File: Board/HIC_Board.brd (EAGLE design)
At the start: 52 x 37.5 mm, 104 parts, among them IC1 CXA2075, IC2 4069UBF, IC3 LM358D, IC4 FMW1A, IC5 FMW1A, IC6 IMN10A, Q1 2SA1037, Q2 2SC2411k

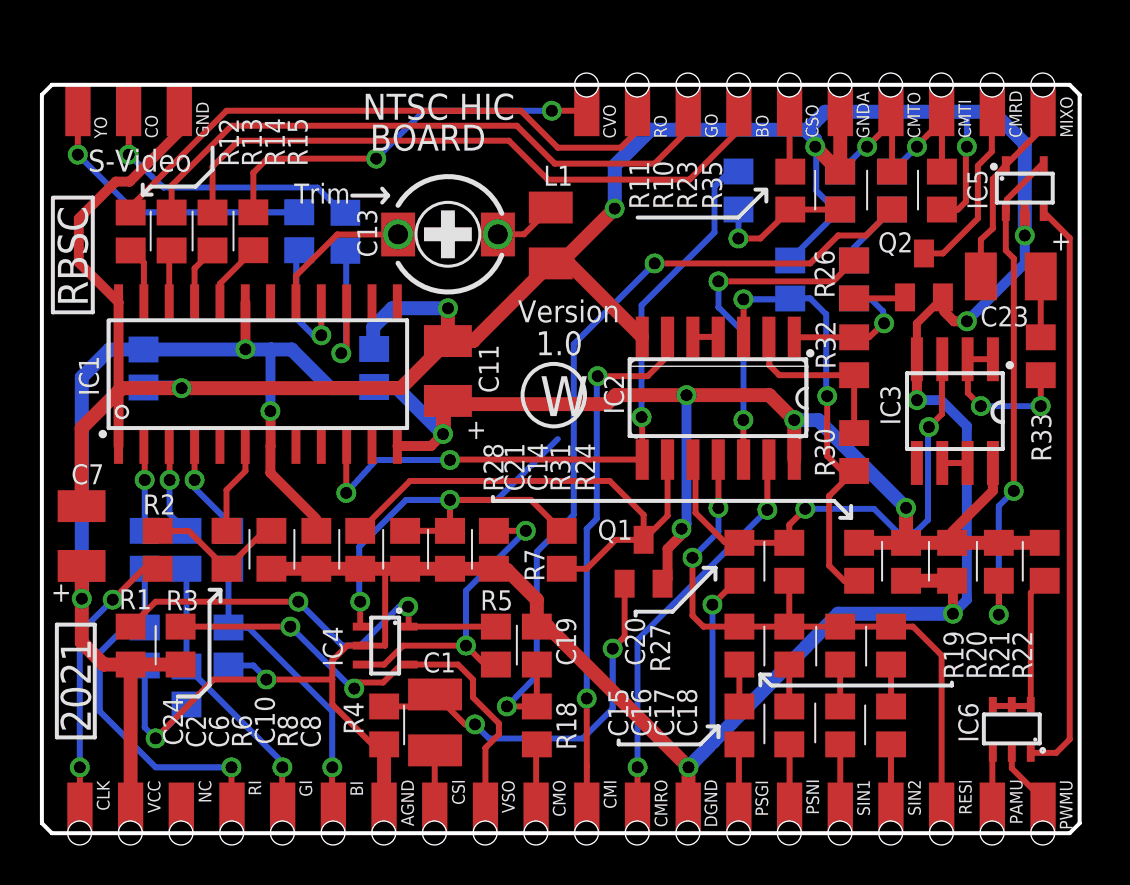
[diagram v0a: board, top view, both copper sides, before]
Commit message: Updated 21.09.2023
Updated to v1.2. The error was fixed, the resistor was added for HB-F1XDJ computer (see the readme file)
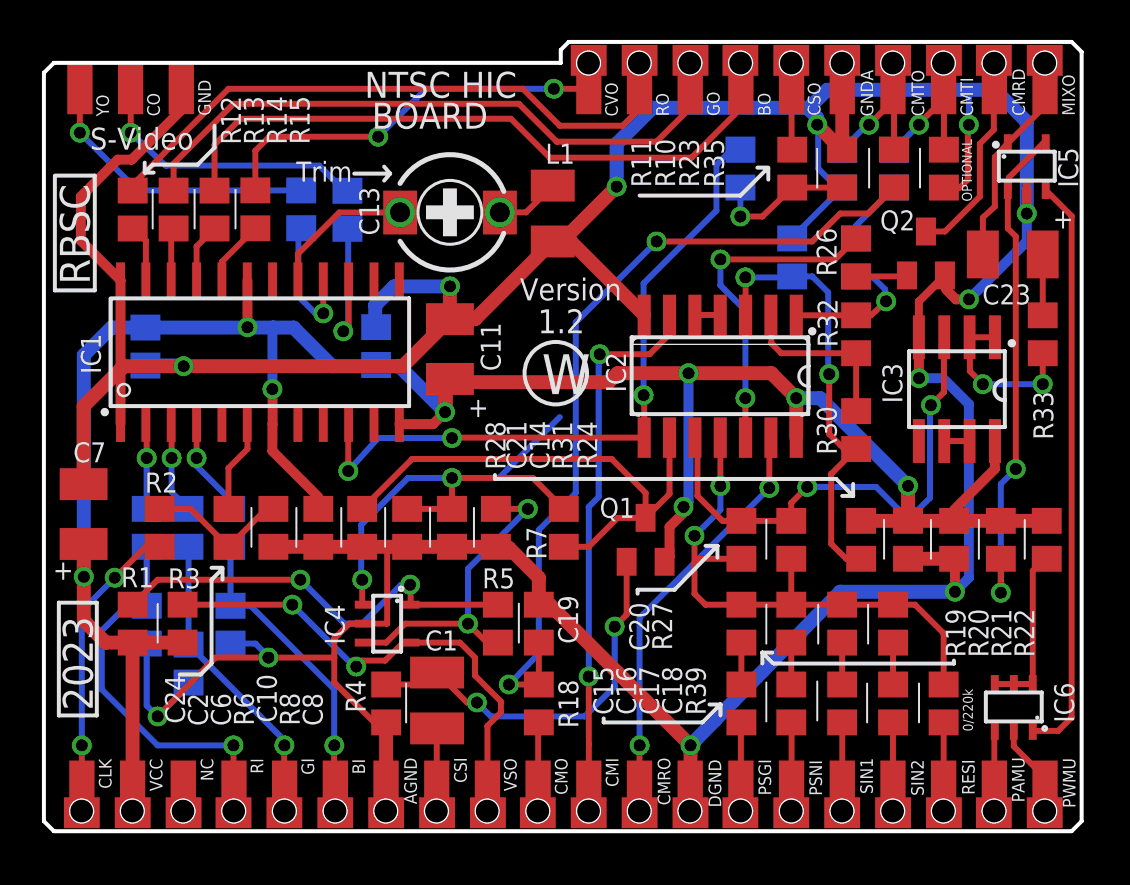
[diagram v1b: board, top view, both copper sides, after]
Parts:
- added R39: 220k, rcl:R0805
- C20: value 10nF -> 39pF
- moved BO 1.10 mm to (35.0, 37.3)
- moved C10 1.10 mm to (18.3, 15.3)
- moved C11 1.10 mm to (20.4, 24.3)
- moved C12 1.10 mm to (16.7, 24.4)
- moved C2 1.10 mm to (11.6, 15.3)
- moved C23 1.10 mm to (48.6, 29.0)
- moved C24 1.10 mm to (9.35, 15.3)
- moved C3 1.10 mm to (5.25, 15.3)
- moved C4 1.10 mm to (7.34, 15.3)
- moved C5 1.10 mm to (9.44, 15.3)
- moved C6 1.10 mm to (13.8, 15.3)
- moved C8 1.10 mm to (22.8, 15.3)
- moved C9 1.10 mm to (5.19, 24.4)
- moved CMRD 1.10 mm to (47.7, 37.3)
- moved CMTI 1.10 mm to (45.2, 37.3)
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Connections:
- new net N$12: R39.1, RESI.1
- net GND: no longer C20.2
- net N$43: now also C20.2; no longer C20.1
- net RESI: now also C20.1, R39.2; no longer RESI.1
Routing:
- net GND: track 237.7 -> 229.1 mm, vias 13 -> 12
- net N$12: track 0.00 -> 3.18 mm
- net RESI: track 31.6 -> 29.0 mm
- net N$14: track 14.8 -> 14.1 mm
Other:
- board size 52 x 37.5 mm -> 52 x 39.5 mm
- board text added: "0/220k"
- board text added: "1.2"
- board text added: "2023"
- board text added: "OPTIONAL"
- board text added: "RBSC 2023"
- board text added: "Version 1.2"
- board text removed: "1.0"
- board text removed: "2021"
- board text removed: "RBSC 2021"
- board text removed: "Version 1.0"
